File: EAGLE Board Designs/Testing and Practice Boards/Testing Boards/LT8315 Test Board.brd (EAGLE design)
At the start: 100 x 80 mm, 21 parts, among them T1 TRANSFORMER(3W), U1 LT8315

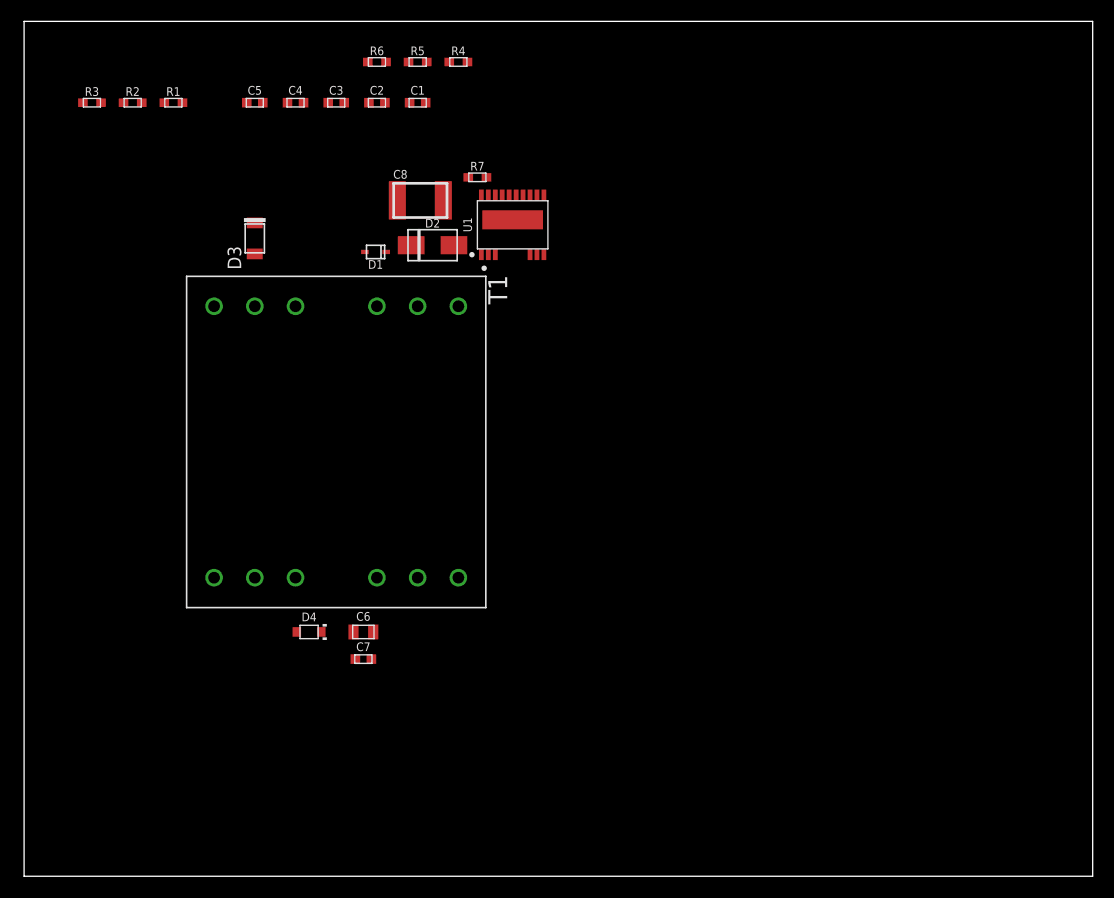
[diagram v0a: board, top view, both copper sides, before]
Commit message: Finished schem and started board
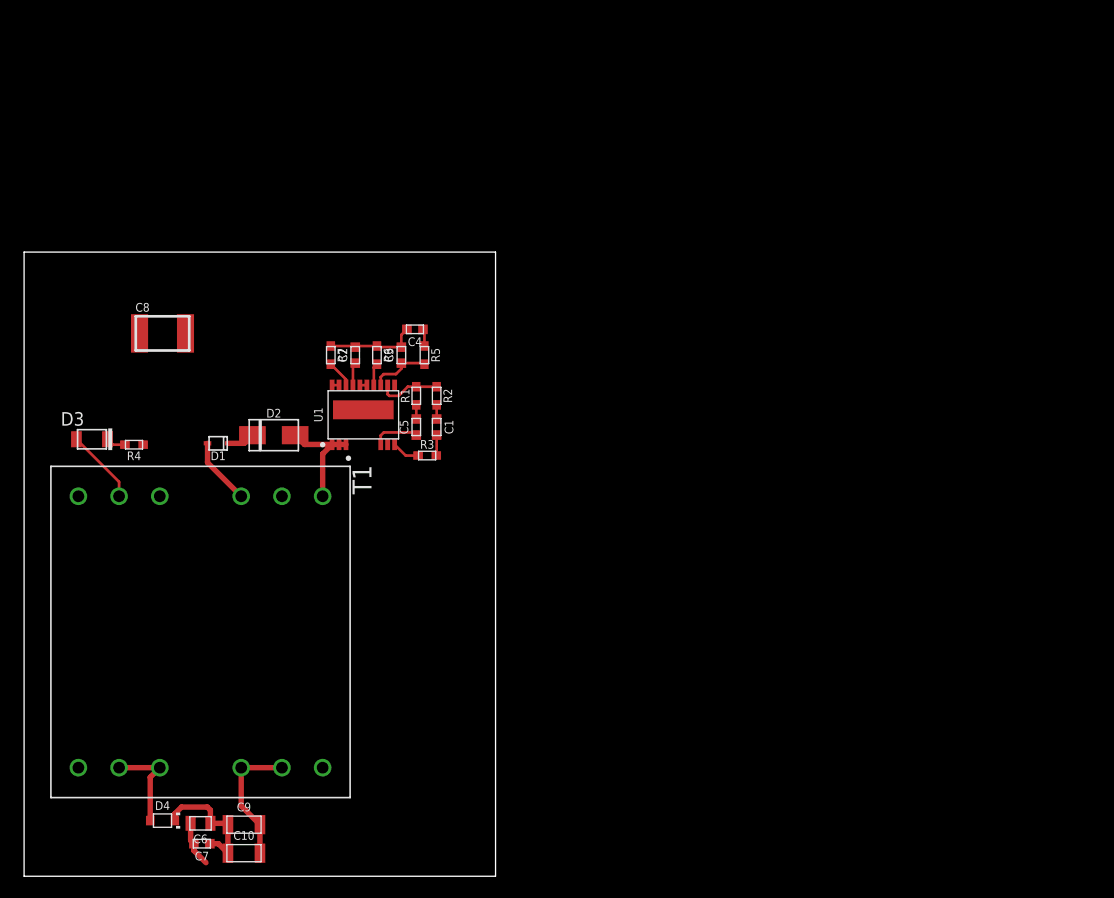
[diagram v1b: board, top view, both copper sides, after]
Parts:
- added C10, C9: CAPACITOR_1206_25V_33UF, HyTechDevices:1206-CAP
- moved R4 46.9 mm to (10.3, 40.4), turned to 180 degrees
- moved R3 45.5 mm to (37.7, 39.4)
- moved R2 39.5 mm to (38.6, 45.0), turned to 270 degrees
- moved R1 35.6 mm to (36.7, 45.0), turned to 90 degrees
- moved C5 33.9 mm to (36.7, 42.0), turned to 90 degrees
- moved C1 30.4 mm to (38.6, 42.0), turned to 270 degrees
- moved R5 27.4 mm to (37.5, 48.8), turned to 270 degrees
- moved R6 27.4 mm to (33.0, 48.8), turned to 270 degrees
- moved C8 27.2 mm to (13.0, 50.8)
- moved C3 24.4 mm to (35.3, 48.8), turned to 90 degrees
- moved D3 24.2 mm to (6.35, 40.9), turned to 0 degrees
- moved C4 24.0 mm to (36.6, 51.2), turned to 180 degrees
- moved C2 23.7 mm to (31.0, 48.8), turned to 90 degrees
- moved C6 23.5 mm to (16.5, 4.95), turned to 180 degrees
- moved D1 23.2 mm to (18.2, 40.5)
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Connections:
- net N$15: now also C10.1, C9.1
- net N$16: now also C10.2, C9.2
- net N$2: no longer C8.2
- net TS-UNFUSED: now also C8.2
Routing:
- net N$16: track 0.00 -> 16.8 mm
- net N$15: track 0.00 -> 12.0 mm
- net TS-UNFUSED: track 0.00 -> 11.2 mm
- net N$2: track 0.00 -> 10.3 mm
- net N$13: track 0.00 -> 9.13 mm
- net N$5: track 0.00 -> 8.31 mm
- net TS+UNFUSED: track 0.00 -> 6.26 mm
- net N$4: track 0.00 -> 5.85 mm
- net N$10: track 0.00 -> 5.73 mm
- net N$12: track 0.00 -> 4.39 mm
- net N$7: track 0.00 -> 2.62 mm
- net N$8: track 0.00 -> 2.55 mm
- net N$1: track 0.00 -> 2.53 mm
- net N$9: track 0.00 -> 2.15 mm
- net N$11: track 0.00 -> 2.09 mm
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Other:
- board size 100 x 80 mm -> 44.1 x 58.4 mm

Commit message: Made more changes to board and schematic
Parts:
- added D5: LED_0603_GREEN, HyTechDevices:0603-LED
- added J1, J2: CONNECTOR-2_μF_T_V_BLACK, HyTechDevices:MOLEX_MICROFIT_PTH_VERTICAL_02_DUAL
- added R8: RESISTOR_0603_1K, HyTechDevices:0603-RES
- added TP1, TP2, TP3, TP4, TP5: TEST_POINT, HyTechDevices:5015
- moved R4 8.07 mm to (7.62, 48.0)
- moved D3 7.95 mm to (3.68, 48.4)
- moved C4 7.62 mm to (36.6, 58.8)
- moved D1 7.62 mm to (18.2, 48.1)
- moved D2 7.62 mm to (23.4, 48.9)
- moved R1 7.62 mm to (36.7, 52.6)
- moved R2 7.62 mm to (38.6, 52.6)
- moved R3 7.62 mm to (37.7, 47.0)
- moved T1 7.62 mm to (16.5, 30.5)
- moved C10 7.62 mm to (20.6, 9.78)
- moved C6 7.62 mm to (16.5, 12.6)
- moved C9 7.62 mm to (20.6, 12.4)
- moved D4 7.62 mm to (13.0, 12.8)
- moved C7 7.62 mm to (16.6, 10.7)
- moved C1 7.62 mm to (38.6, 49.7)
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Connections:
- removed net N$16: C10.2, C6.2, C7.2, C9.2, T1.10, T1.11
- new net +5V: C10.1, C6.1, C7.1, C9.1, D4.C, J2.1, R8.2, TP4.1
- new net GND: C10.2, C6.2, C7.2, C9.2, D5.1, J2.2, T1.10, T1.11, TP5.1
- net N$15: now also D5.2, R8.1; no longer C10.1, C6.1, C7.1, C9.1, D4.C
- net N$9: now also TP1.1
- net TS+UNFUSED: now also J1.1, TP2.1
- net TS-UNFUSED: now also J1.2, TP3.1
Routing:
- net TS-UNFUSED: track 11.2 -> 78.9 mm
- net GND: track 0.00 -> 52.8 mm
- net N$9: track 2.15 -> 50.4 mm, vias 0 -> 3
- net N$5: track 8.31 -> 53.8 mm, vias 0 -> 2
- net +5V: track 0.00 -> 42.5 mm, vias 0 -> 1
- net TS+UNFUSED: track 6.26 -> 24.3 mm
- net N$16: track 16.8 -> 0.00 mm
- net N$15: track 12.0 -> 2.13 mm
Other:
- board size 44.1 x 58.4 mm -> 41.6 x 63.5 mm

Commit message: Added BOMs and finished board
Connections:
- net +5V renamed +12V
- net N$9 renamed AUX
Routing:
- net TS-UNFUSED: track 78.9 -> 79.8 mm
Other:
- board text added: "+12V"
- board text added: "AUX"
- board text added: "GND"
- board text added: "TS+"
- board text added: "TS-"
